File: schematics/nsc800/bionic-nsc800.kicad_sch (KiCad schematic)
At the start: 8 parts, among them J1 Bionic-P135, J2 Bionic-P245, U1 NSC800N, U2 11AA010-I/TT

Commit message: [schematics] Update LED footprint
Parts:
- D1: footprint 0-LocalLibrary:LED_CSL1901UW1_ROM -> 0-LocalLibrary:LED_CSL1901UW1_ROM-M
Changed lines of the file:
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@@
 			)
 		)
-		(property "Description" ""
+		(property "Description" "Special symbol for telling ERC where power comes from"
 			(at 198.12 46.99 0)
 			(effects
@@
 			)
 		)
-		(property "Description" ""
+		(property "Description" "Special symbol for telling ERC where power comes from"
 			(at 207.01 46.99 0)
 			(effects
@@
 			)
 		)
-		(property "Description" ""
+		(property "Description" "Power symbol creates a global label with name \"GND\" , ground"
 			(at 198.12 46.99 0)
 			(effects
@@
 			)
 		)
-		(property "Description" ""
+		(property "Description" "Power symbol creates a global label with name \"GND\" , ground"
 			(at 80.01 137.16 0)
 			(effects
@@
 			)
 		)
-		(property "Description" ""
+		(property "Description" "Power symbol creates a global label with name \"GND\" , ground"
 			(at 207.01 87.63 0)
 			(effects
@@
 			)
 		)
-		(property "Description" ""
+		(property "Description" "Power symbol creates a global label with name \"GND\" , ground"
 			(at 215.9 59.69 0)
 			(effects
@@
 			)
 		)
-		(property "Description" ""
+		(property "Description" "Power symbol creates a global label with name \"VCC\""
 			(at 207.01 46.99 0)
 			(effects
@@
 			)
 		)
-		(property "Footprint" "0-LocalLibrary:LED_CSL1901UW1_ROM"
+		(property "Footprint" "0-LocalLibrary:LED_CSL1901UW1_ROM-M"
 			(at 207.01 50.8 0)
 			(effects
@@
 			)
 		)
-		(property "Description" ""
+		(property "Description" "Red LED (Low Current Emission, SMD)"
 			(at 215.9 46.99 0)
 			(effects
@@
 			)
 		)
-		(property "Description" ""
+		(property "Description" "Power symbol creates a global label with name \"VCC\""
 			(at 215.9 46.99 0)
 			(effects
@@
 			)
 		)
-		(property "Description" ""
+		(property "Description" "Power symbol creates a global label with name \"GND\" , ground"
 			(at 161.29 133.35 0)
 			(effects
@@
 			)
 		)
-		(property "Description" ""
+		(property "Description" "Power symbol creates a global label with name \"VCC\""
 			(at 207.01 82.55 0)
 			(effects
@@
 			)
 		)
-		(property "Description" ""
+		(property "Description" "Resistor, small symbol"
 			(at 215.9 57.15 0)
 			(effects
@@
 			)
 		)
-		(property "Description" ""
+		(property "Description" "Power symbol creates a global label with name \"VCC\""
 			(at 177.8 74.93 0)
 			(effects
@@
 			)
 		)
-		(property "Description" ""
+		(property "Description" "Power symbol creates a global label with name \"VCC\""
 			(at 80.01 130.81 0)
 			(effects

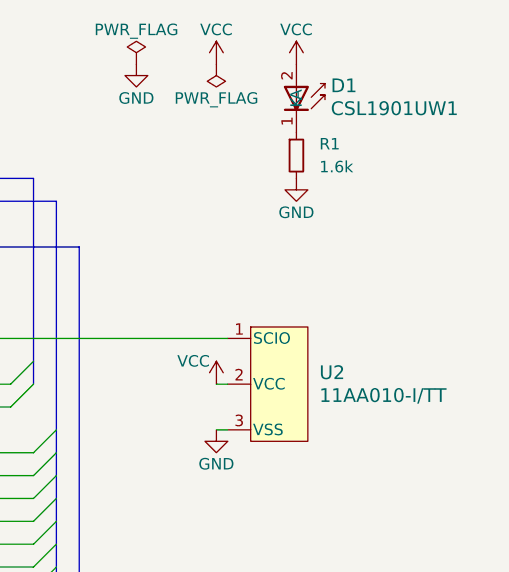
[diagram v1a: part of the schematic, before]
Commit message: [NSC800] Cleanup schematics
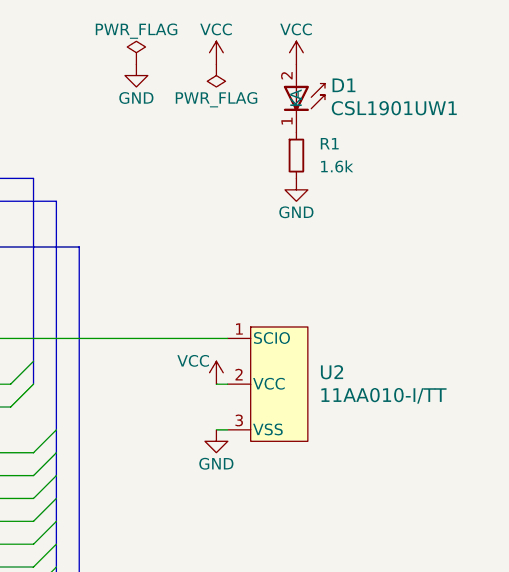
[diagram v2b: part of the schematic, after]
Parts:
- D1: footprint 0-LocalLibrary:LED_CSL1901UW1_ROM-M -> rhom:LED_CSL1901UW1_ROM-M; symbol 0-LocalLibrary:CSL1901UW1 -> rhom:CSL1901UW1
- J1: footprint 0-LocalLibrary:Bionic-P135_Vertical -> bionic:Bionic-P135_Vertical; symbol 0-LocalLibrary:Bionic-P135 -> bionic:Bionic-P135
- J2: footprint 0-LocalLibrary:Bionic-P245_Vertical -> bionic:Bionic-P245_Vertical; symbol 0-LocalLibrary:Bionic-P245 -> bionic:Bionic-P245
- U1: footprint 0-LocalLibrary:DIP-40_W15.24mm_Socket -> bionic:DIP-40_W15.24mm_Socket; symbol 0-LocalLibrary:NSC800N -> cpu:NSC800N
- U2: footprint 0-LocalLibrary:SOT-23_MC_MCH-M -> microchip:SOT-23_MC_MCH-M; symbol 0-LocalLibrary:11AA010-I_TT -> microchip:11AA010-I_TT
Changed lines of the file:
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@@
 	)
 	(symbol
-		(lib_id "0-LocalLibrary:Bionic-P245")
+		(lib_id "bionic:Bionic-P245")
 		(at 175.26 102.87 0)
 		(unit 1)
@@
 			)
 		)
-		(property "Footprint" "0-LocalLibrary:Bionic-P245_Vertical"
+		(property "Footprint" "bionic:Bionic-P245_Vertical"
 			(at 176.53 138.43 0)
 			(effects
@@
 			)
 		)
-		(property "Description" ""
+		(property "Description" "Generic connector, single row, 01x24, script generated (kicad-library-utils/schlib/autogen/connector/)"
 			(at 175.26 102.87 0)
 			(effects
@@
 	)
 	(symbol
-		(lib_id "0-LocalLibrary:NSC800N")
+		(lib_id "cpu:NSC800N")
 		(at 96.52 105.41 0)
 		(unit 1)
@@
 			)
 		)
-		(property "Footprint" "0-LocalLibrary:DIP-40_W15.24mm_Socket"
+		(property "Footprint" "bionic:DIP-40_W15.24mm_Socket"
 			(at 97.79 139.7 0)
 			(effects
@@
 			)
 		)
-		(property "Description" ""
+		(property "Description" "8-bit General Purpose Microprocessor, DIP-40"
 			(at 96.52 105.41 0)
 			(effects
@@
 	)
 	(symbol
-		(lib_id "0-LocalLibrary:CSL1901UW1")
+		(lib_id "rhom:CSL1901UW1")
 		(at 215.9 46.99 270)
 		(unit 1)
@@
 		(fields_autoplaced yes)
 		(property "Reference" "D1"
-			(at 219.71 49.403 90)
+			(at 219.71 49.4029 90)
 			(effects
 				(font
@@
 		)
 		(property "Value" "CSL1901UW1"
-			(at 219.71 51.943 90)
+			(at 219.71 51.9429 90)
 			(effects
 				(font
@@
 			)
 		)
-		(property "Footprint" "0-LocalLibrary:LED_CSL1901UW1_ROM-M"
+		(property "Footprint" "rhom:LED_CSL1901UW1_ROM-M"
 			(at 207.01 50.8 0)
 			(effects
@@
 	)
 	(symbol
-		(lib_id "0-LocalLibrary:Bionic-P135")
+		(lib_id "bionic:Bionic-P135")
 		(at 167.64 102.87 0)
 		(unit 1)
@@
 			)
 		)
-		(property "Footprint" "0-LocalLibrary:Bionic-P135_Vertical"
+		(property "Footprint" "bionic:Bionic-P135_Vertical"
 			(at 168.91 138.43 0)
 			(effects
@@
 			)
 		)
-		(property "Description" ""
+		(property "Description" "Generic connector, single row, 01x24, script generated (kicad-library-utils/schlib/autogen/connector/)"
 			(at 167.64 102.87 0)
 			(effects
@@
 	)
 	(symbol
-		(lib_id "0-LocalLibrary:11AA010-I_TT")
+		(lib_id "microchip:11AA010-I_TT")
 		(at 210.82 76.2 0)
 		(unit 1)
@@
 		(fields_autoplaced yes)
 		(property "Reference" "U2"
-			(at 218.44 81.28 0)
+			(at 218.44 81.2799 0)
 			(effects
 				(font
@@
 		)
 		(property "Value" "11AA010-I/TT"
-			(at 218.44 83.82 0)
+			(at 218.44 83.8199 0)
 			(effects
 				(font
@@
 			)
 		)
-		(property "Footprint" "0-LocalLibrary:SOT-23_MC_MCH-M"
+		(property "Footprint" "microchip:SOT-23_MC_MCH-M"
 			(at 213.36 93.98 0)
 			(effects
@@
 			)
 		)
-		(property "Description" ""
+		(property "Description" "UNI/O Serial EEPROM (1Kbit)"
 			(at 210.82 76.2 0)
 			(effects

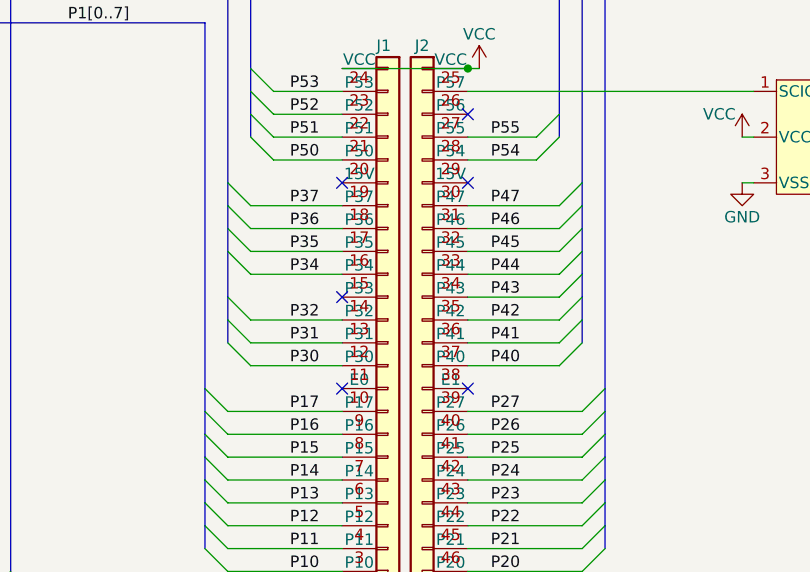
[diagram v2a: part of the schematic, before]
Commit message: [NSC800] Update schematics
Remove unused pins from bionic connector
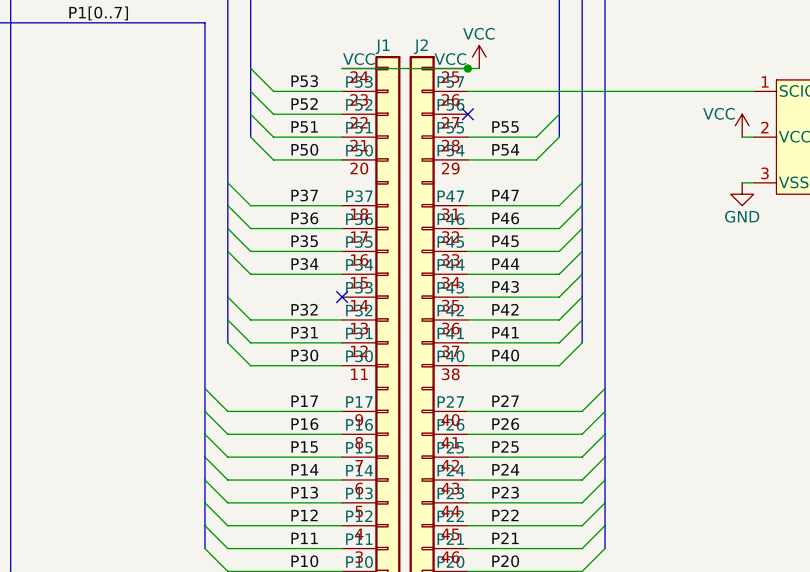
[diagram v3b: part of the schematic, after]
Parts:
- J1: footprint bionic:Bionic-P135_Vertical -> bionic:Bionic-P135_THT
- J2: footprint bionic:Bionic-P245_Vertical -> bionic:Bionic-P245_THT
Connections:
- no-connect marks 7 -> 3
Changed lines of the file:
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@@
 	(title_block
 		(title "BionicNSC800")
-		(date "2024-11-02")
-		(rev "3")
+		(date "2025-03-02")
+		(rev "4")
 		(company "Tadashi G. Takaoka")
 	)
@@
 	)
 	(no_connect
-		(at 176.53 87.63)
-	)
-	(no_connect
-		(at 162.56 110.49)
-	)
-	(no_connect
-		(at 162.56 87.63)
-	)
-	(no_connect
 		(at 176.53 80.01)
 	)
 	(no_connect
-		(at 176.53 110.49)
-	)
-	(no_connect
 		(at 162.56 100.33)
 	)
@@
 			)
 		)
-		(property "Footprint" "bionic:Bionic-P245_Vertical"
+		(property "Footprint" "bionic:Bionic-P245_THT"
 			(at 176.53 138.43 0)
 			(effects
@@
 		(pin "41"
 		)
-		(pin "30"
-		)
 		(pin "31"
 		)
@@
 		(pin "37"
 		)
-		(pin "39"
-		)
 		(pin "48"
 		)
@@
 			)
 		)
-		(property "Footprint" "bionic:Bionic-P135_Vertical"
+		(property "Footprint" "bionic:Bionic-P135_THT"
 			(at 168.91 138.43 0)
 			(effects
@@
 		(pin "15"
 		)
-		(pin "10"
-		)
 		(pin "13"
 		)
@@
 		(pin "8"
 		)
-		(pin "19"
-		)
 		(pin "12"
